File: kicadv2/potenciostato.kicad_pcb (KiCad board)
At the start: 2 copper layers, 100 x 100 mm, 46 parts, among them J1 Conn_01x03_Female, J10 Conn_01x01_Female, J11 Conn_01x01_Female, J12 Conn_01x01_Female, J2 USB_B_Micro, J3 Conn_01x03_Male, J4 Conn_01x01_Female, J5 Conn_01x01_Female, J6 Conn_01x01_Female, J7 Conn_01x01_Female, J8 Conn_01x01_Female, J9 Conn_01x01_Female, U1 OP77, U2 TL082, U3 OP77, U4 OP77, U7 TL064

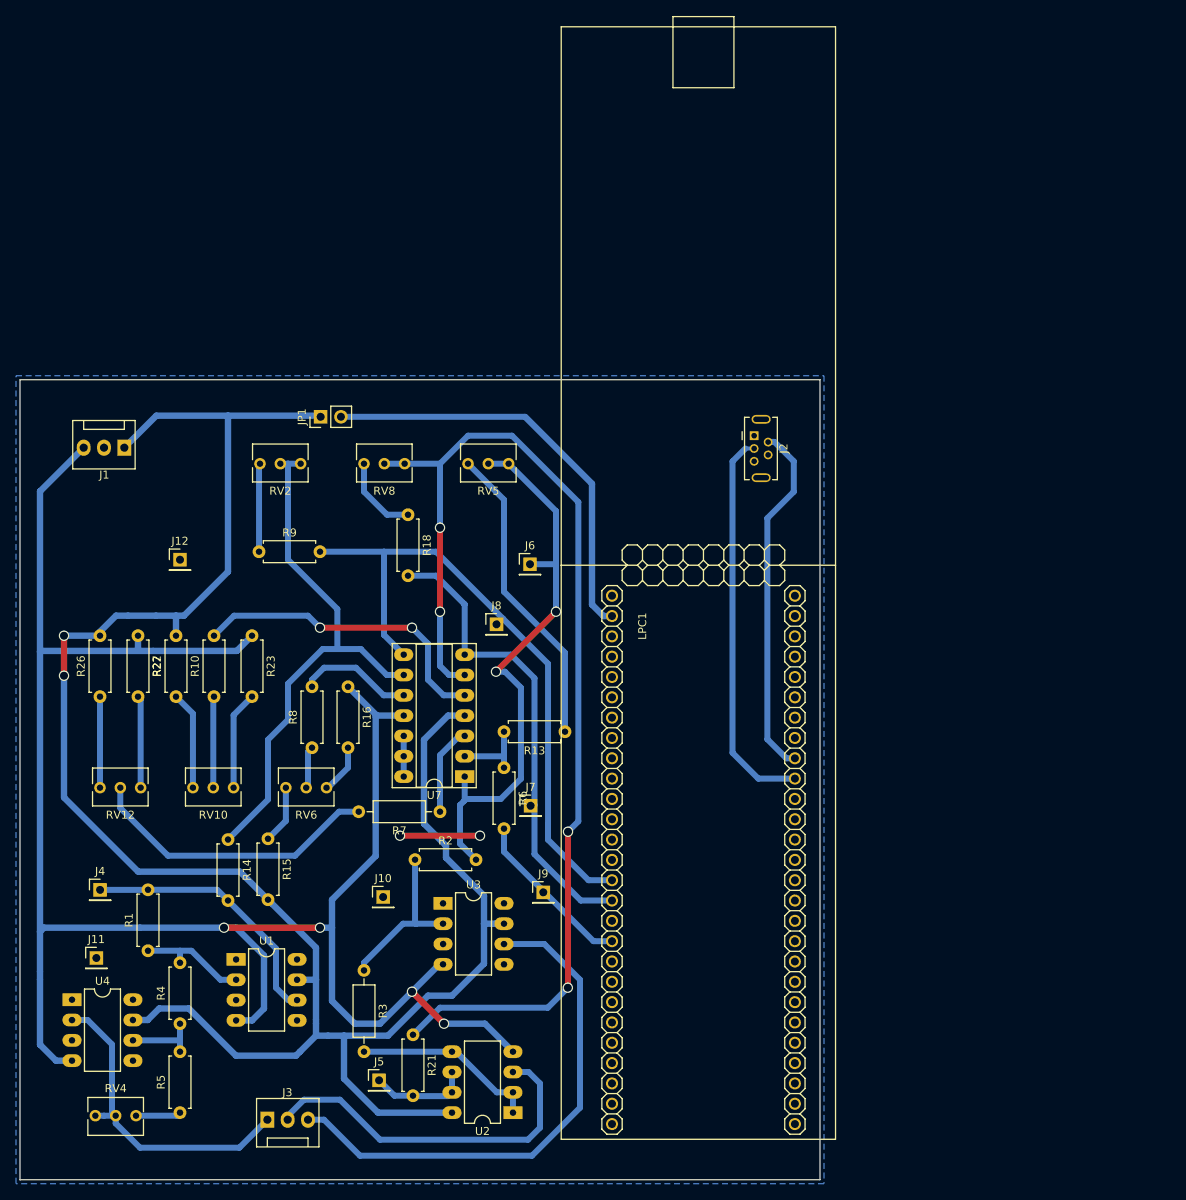
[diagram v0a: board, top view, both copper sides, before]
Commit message: se agregan huellas smd
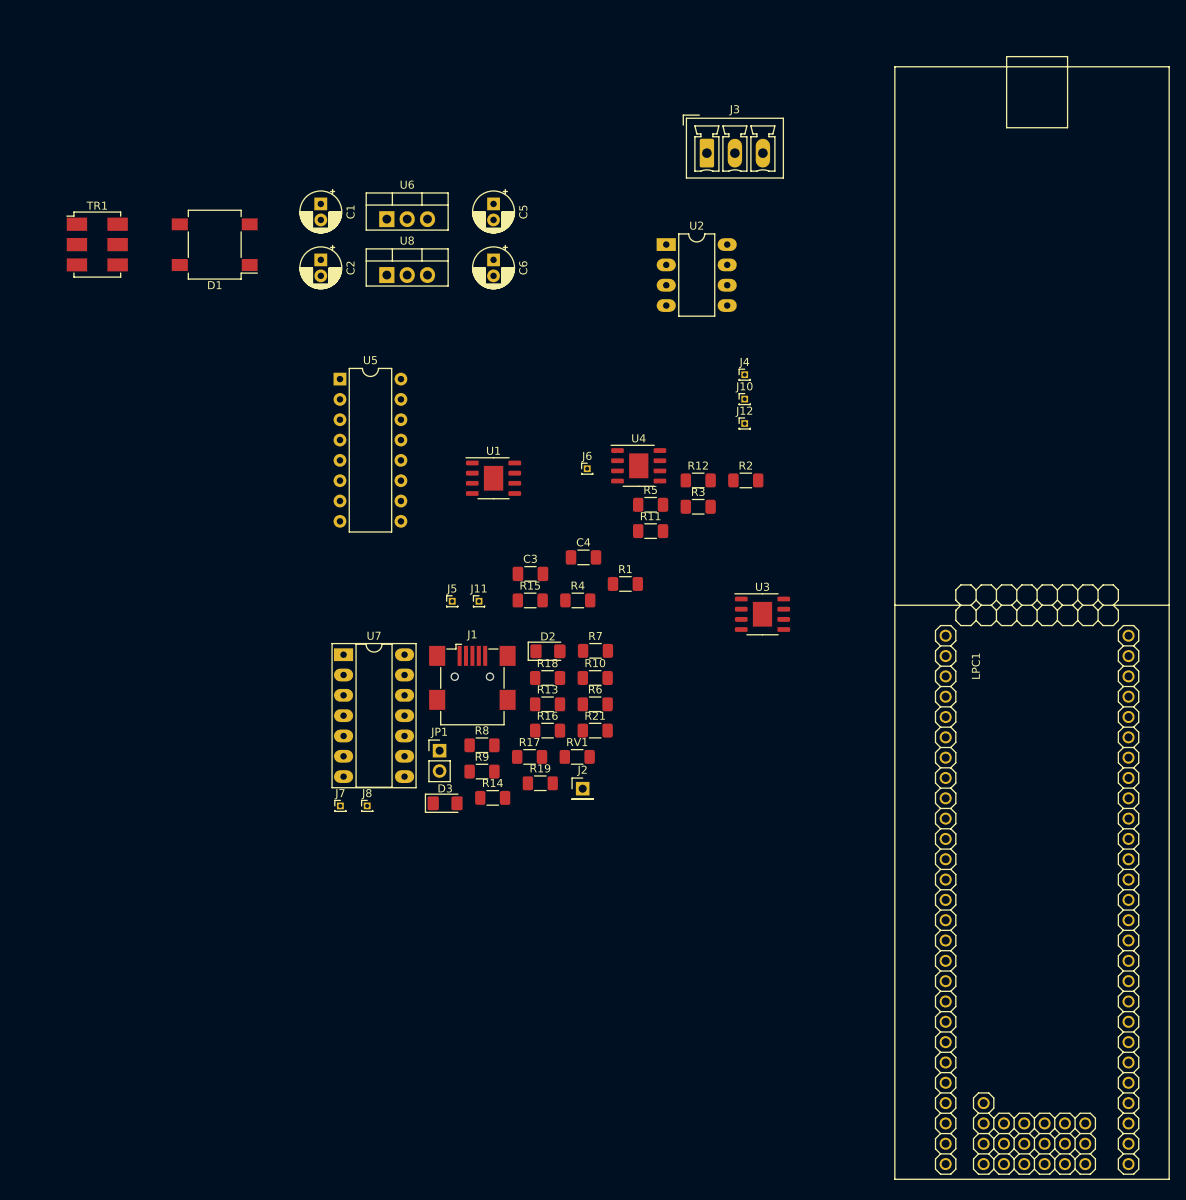
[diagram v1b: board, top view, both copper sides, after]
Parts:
- removed J9: Conn_01x01_Female, Connector_PinHeader_2.54mm:PinHeader_1x01_P2.54mm_Vertical
- removed R22, R26: 10K, Resistor_THT:R_Axial_DIN0207_L6.3mm_D2.5mm_P7.62mm_Horizontal
- removed R23: 15K, Resistor_THT:R_Axial_DIN0207_L6.3mm_D2.5mm_P7.62mm_Horizontal
- removed R27: 1K, Resistor_THT:R_Axial_DIN0207_L6.3mm_D2.5mm_P7.62mm_Horizontal
- removed RV10, RV12, RV4, RV6, RV8: 1K, Potentiometer_THT:Potentiometer_Bourns_3266Y_Vertical
- removed RV2, RV5: R_POT, Potentiometer_THT:Potentiometer_Bourns_3266Y_Vertical
- added C1: 10uF, Capacitor_THT:CP_Radial_D5.0mm_P2.00mm, F.Cu at (110.5, 33.0)
- added C2: 10uF, Capacitor_THT:CP_Radial_D5.0mm_P2.00mm, F.Cu at (110.5, 40.0)
- added C3: 100nF, Capacitor_SMD:C_1206_3216Metric_Pad1.33x1.80mm_HandSolder, F.Cu at (136.7, 79.3)
- added C4: 100nF, Capacitor_SMD:C_1206_3216Metric_Pad1.33x1.80mm_HandSolder, F.Cu at (143.3, 77.2)
- added C5: 10uF, Capacitor_THT:CP_Radial_D5.0mm_P2.00mm, F.Cu at (132.1, 33.0)
- added C6: 10uF, Capacitor_THT:CP_Radial_D5.0mm_P2.00mm, F.Cu at (132.1, 40.0)
- added D1: D_Bridge_+-AA, Diode_SMD:Diode_Bridge_Vishay_DFS, F.Cu at (97.2, 38.1)
- added D2: 1N4007, Diode_SMD:D_1206_3216Metric_Pad1.42x1.75mm_HandSolder, F.Cu at (138.9, 88.9)
- added D3: 1N4007, Diode_SMD:D_1206_3216Metric_Pad1.42x1.75mm_HandSolder, F.Cu at (126.0, 107.9)
- added R11: 100K, Resistor_SMD:R_1206_3216Metric_Pad1.30x1.75mm_HandSolder, F.Cu at (151.7, 73.9)
- added R12: 4K7, Resistor_SMD:R_1206_3216Metric_Pad1.30x1.75mm_HandSolder, F.Cu at (157.7, 67.6)
- added R17: 4K7, Resistor_SMD:R_1206_3216Metric_Pad1.30x1.75mm_HandSolder, F.Cu at (136.6, 102.1)
- added R19: 5K6, Resistor_SMD:R_1206_3216Metric_Pad1.30x1.75mm_HandSolder, F.Cu at (137.9, 105.4)
- added RV1: 10K, Resistor_SMD:R_1206_3216Metric_Pad1.30x1.75mm_HandSolder, F.Cu at (142.5, 102.1)
- added TR1: ADT2-71T, RF_Mini-Circuits:Mini-Circuits_CD637_H5.23mm, F.Cu at (82.5, 38.1)
- added U5: 4316, Package_DIP:DIP-16_W7.62mm, F.Cu at (112.9, 54.9)
- added U6: L7805, Package_TO_SOT_THT:TO-220-3_Vertical, F.Cu at (118.7, 34.9)
- added U8: L7905, Package_TO_SOT_THT:TO-220-3_Vertical, F.Cu at (118.7, 41.9)
- J1: value Conn_01x03_Female -> USB_B_Micro; footprint Connector:FanPinHeader_1x03_P2.54mm_Vertical -> Connector_USB:USB_Mini-B_Wuerth_65100516121_Horizontal
- J10, J11, J12: value Conn_01x01_Female -> test_GND; footprint Connector_PinHeader_2.54mm:PinHeader_1x01_P2.54mm_Vertical -> Connector_PinHeader_1.00mm:PinHeader_1x01_P1.00mm_Vertical
- J2: value USB_B_Micro -> test_DAC; footprint Connector_USB:USB_Mini-B_Tensility_54-00023_Vertical -> Connector_PinHeader_2.54mm:PinHeader_1x01_P2.54mm_Vertical
- J3: footprint Connector:FanPinHeader_1x03_P2.54mm_Vertical -> Connector_Phoenix_MC:PhoenixContact_MCV_1,5_3-G-3.5_1x03_P3.50mm_Vertical
- J4, J7: value Conn_01x01_Female -> test_I; footprint Connector_PinHeader_2.54mm:PinHeader_1x01_P2.54mm_Vertical -> Connector_PinHeader_1.00mm:PinHeader_1x01_P1.00mm_Vertical
- J5, J8: value Conn_01x01_Female -> test_V; footprint Connector_PinHeader_2.54mm:PinHeader_1x01_P2.54mm_Vertical -> Connector_PinHeader_1.00mm:PinHeader_1x01_P1.00mm_Vertical
- J6: value Conn_01x01_Female -> test_DAC; footprint Connector_PinHeader_2.54mm:PinHeader_1x01_P2.54mm_Vertical -> Connector_PinHeader_1.00mm:PinHeader_1x01_P1.00mm_Vertical
- JP1: value Jumper -> alimentacion_lpc
- LPC1: footprint LPC:LPCXPRESSO_LPC1769 -> kicadv2:LPCXPRESSO_LPC1769
- R1: value 15K -> 1K; footprint Resistor_THT:R_Axial_DIN0207_L6.3mm_D2.5mm_P7.62mm_Horizontal -> Resistor_SMD:R_1206_3216Metric_Pad1.30x1.75mm_HandSolder
- R10, R15, R2, R21: footprint Resistor_THT:R_Axial_DIN0207_L6.3mm_D2.5mm_P7.62mm_Horizontal -> Resistor_SMD:R_1206_3216Metric_Pad1.30x1.75mm_HandSolder
- R13: value 4K7 -> 5K6; footprint Resistor_THT:R_Axial_DIN0207_L6.3mm_D2.5mm_P7.62mm_Horizontal -> Resistor_SMD:R_1206_3216Metric_Pad1.30x1.75mm_HandSolder
- R14, R4, R6, R8: value 1K -> 10K; footprint Resistor_THT:R_Axial_DIN0207_L6.3mm_D2.5mm_P7.62mm_Horizontal -> Resistor_SMD:R_1206_3216Metric_Pad1.30x1.75mm_HandSolder
- R16: value 1K -> 5K6; footprint Resistor_THT:R_Axial_DIN0207_L6.3mm_D2.5mm_P7.62mm_Horizontal -> Resistor_SMD:R_1206_3216Metric_Pad1.30x1.75mm_HandSolder
- R18, R9: value 4K7 -> 10K; footprint Resistor_THT:R_Axial_DIN0207_L6.3mm_D2.5mm_P7.62mm_Horizontal -> Resistor_SMD:R_1206_3216Metric_Pad1.30x1.75mm_HandSolder
- R3: footprint Resistor_THT:R_Axial_DIN0207_L6.3mm_D2.5mm_P10.16mm_Horizontal -> Resistor_SMD:R_1206_3216Metric_Pad1.30x1.75mm_HandSolder
- R5: value 1M -> 6K8; footprint Resistor_THT:R_Axial_DIN0207_L6.3mm_D2.5mm_P7.62mm_Horizontal -> Resistor_SMD:R_1206_3216Metric_Pad1.30x1.75mm_HandSolder
- R7: value 1K -> 10K; footprint Resistor_THT:R_Axial_DIN0207_L6.3mm_D2.5mm_P10.16mm_Horizontal -> Resistor_SMD:R_1206_3216Metric_Pad1.30x1.75mm_HandSolder
- U1, U3, U4: footprint Package_DIP:DIP-8_W7.62mm_LongPads -> Package_SO:HSOP-8-1EP_3.9x4.9mm_P1.27mm_EP2.41x3.1mm
- moved J3 132.7 mm to (158.8, 26.7)
- moved U2 110.2 mm to (153.7, 38.1), turned to 0 degrees
- moved J4 103.1 mm to (163.5, 54.4)
- moved U4 97.3 mm to (150.2, 65.8)
- moved R5 96.1 mm to (151.7, 70.6), turned to 0 degrees
- moved J10 76.9 mm to (163.5, 57.4)
- moved R1 75.3 mm to (148.6, 80.5), turned to 0 degrees
- moved J12 72.6 mm to (163.5, 60.5)
- moved R4 72.6 mm to (142.6, 82.6), turned to 0 degrees
- moved R3 71.4 mm to (157.7, 70.9), turned to 0 degrees
- moved U1 68.2 mm to (132.1, 67.3)
- moved J11 65.4 mm to (130.3, 82.7)
- moved R2 62.9 mm to (163.6, 67.6)
- moved J5 60.6 mm to (126.9, 82.7)
- moved U3 53.9 mm to (165.7, 84.3)
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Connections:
- J1 pad 1: +5V -> Net-(J1-Pad1)
- J1 pad 2: GND -> Net-(J1-Pad2)
- J1 pad 3: -5V -> Net-(J1-Pad3)
- J7 pad 1: /LPC/ADC1 -> Net-(J7-Pad1)
- J8 pad 1: /LPC/ADC0 -> Net-(J8-Pad1)
- LPC1 pad 15: /LPC/ADC0 -> Net-(J7-Pad1)
- LPC1 pad 16: /LPC/ADC1 -> Net-(J8-Pad1)
- LPC1 pad 18: /LPC/DAC -> Net-(J2-Pad1)
- LPC1 pad 36: Net-(J2-Pad2) -> Net-(J1-Pad2)
- LPC1 pad 37: Net-(J2-Pad3) -> Net-(J1-Pad3)
- LPC1 pad 47: Net-(LPC1-Pad47) -> /salida_dac/gan_x1
- LPC1 pad 48: Net-(LPC1-Pad48) -> /salida_dac/gan_x5
- LPC1 pad 49: Net-(LPC1-Pad49) -> /salida_dac/gan_x0.1
- LPC1 pad 50: Net-(LPC1-Pad50) -> /salida_dac/gan_x10
- R1 pad 2: /salida_dac/I_IN -> Net-(R1-Pad2)
- R10 pad 1: Net-(R10-Pad1) -> /salida_dac/VOffset
- R13 pad 1: Net-(R13-Pad1) -> /salida_dac/VIN
- R15 pad 1: Net-(R15-Pad1) -> Net-(R1-Pad1)
- R15 pad 2: +5V -> Net-(R15-Pad2)
- R16 pad 1: -5V -> Net-(D2-Pad2)
- R16 pad 2: Net-(R16-Pad2) -> +5V
- R18 pad 2: /LPC/ADC1 -> Net-(J8-Pad1)
- R21 pad 1: Net-(R21-Pad1) -> Net-(R18-Pad1)
- R5 pad 1: Net-(R5-Pad1) -> Net-(J3-Pad1)
- R6 pad 2: /LPC/DAC -> Net-(J2-Pad1)
- R7 pad 2: Net-(R7-Pad2) -> /salida_dac/VOffset
- R8 pad 1: Net-(R8-Pad1) -> /salida_dac/VOffset
- R9 pad 1: Net-(R9-Pad1) -> Net-(R14-Pad1)
- R9 pad 2: /LPC/ADC0 -> Net-(J7-Pad1)
- U7 pad 12: GND -> Net-(RV1-Pad2)
- U7 pad 13: GND -> /salida_dac/VOffset
- U7 pad 14: GND -> /salida_dac/VOffset
- U7 pad 6: Net-(R21-Pad1) -> Net-(R18-Pad1)
- U7 pad 7: /LPC/ADC1 -> Net-(J8-Pad1)
- U7 pad 8: /LPC/ADC0 -> Net-(J7-Pad1)
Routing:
- net +5V: track 260.2 -> 0.00 mm, vias 2 -> 0
- net -5V: track 245.9 -> 0.00 mm, vias 4 -> 0
- net Net-(R21-Pad1): track 141.6 -> 0.00 mm, vias 4 -> 0
- net /LPC/ADC0: track 81.8 -> 0.00 mm
- net /salida_dac/VIN: track 72.3 -> 0.00 mm, vias 2 -> 0
- net Net-(R14-Pad1): track 68.5 -> 0.00 mm
- net Net-(J3-Pad3): track 65.7 -> 0.00 mm
- net /LPC/ADC1: track 59.5 -> 0.00 mm
- net Net-(JP1-Pad2): track 53.1 -> 0.00 mm
- net Net-(J2-Pad3): track 48.9 -> 0.00 mm
- net Net-(J3-Pad2): track 45.0 -> 0.00 mm
- net Net-(J2-Pad2): track 44.8 -> 0.00 mm
- net Net-(J3-Pad1): track 40.5 -> 0.00 mm
- net Net-(R10-Pad2): track 39.2 -> 0.00 mm, vias 2 -> 0
- net Net-(R13-Pad1): track 38.5 -> 0.00 mm
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- removed copper zone on B.Cu, net GND
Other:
- board outline removed
- net class Alimentación added: clearance 0.7, trace_width 0.8, via_dia 1.3, via_drill 1
- net class Default added: clearance 0.7, trace_width 0.75, via_dia 1.3, via_drill 1
- net class Señal added: clearance 0.5, trace_width 0.75, via_dia 1.3, via_drill 1
- net class USB added: clearance 0.2, trace_width 0.5, via_dia 0.7, via_drill 0.5
